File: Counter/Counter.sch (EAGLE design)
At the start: 6 parts

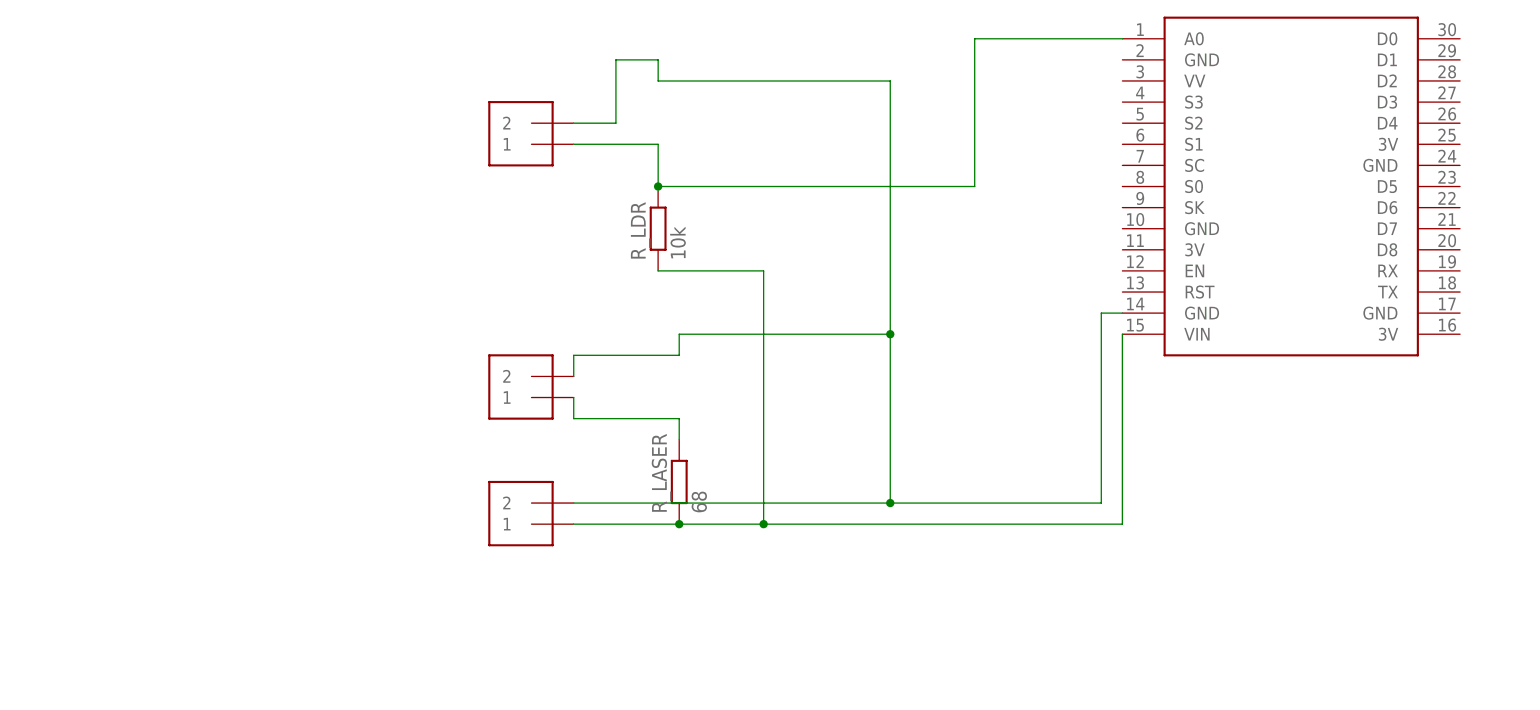
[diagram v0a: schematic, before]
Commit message: revisi rangkaian rev 3 + penambahan reset
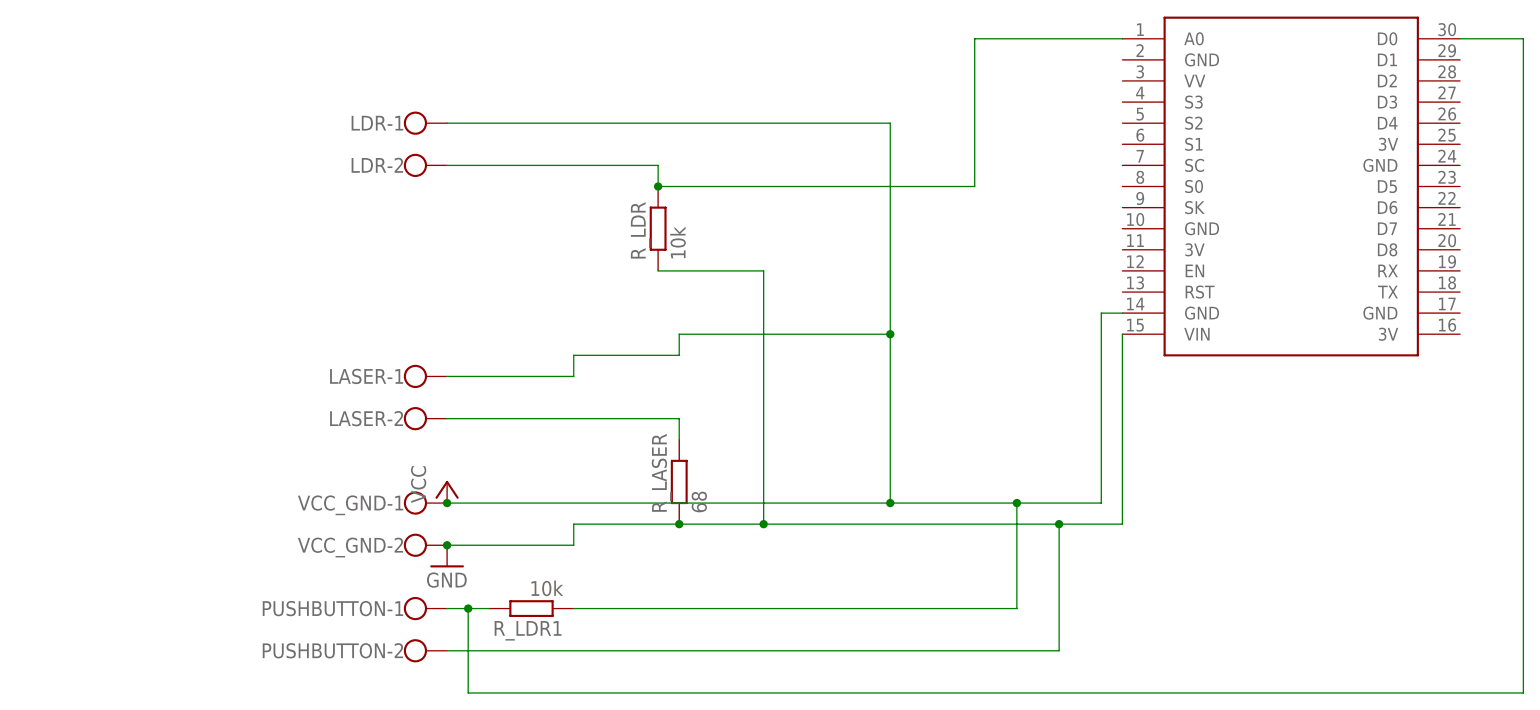
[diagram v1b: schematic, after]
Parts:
- added PUSHBUTTON: (no value), con-wago-500:W237-102
- added R_LDR1: 10k, rcl:R-EU_0207/10
- LASER, LDR, VCC_GND: value 1X2-3.5MM -> (none); device adafruit:1X2-3.5MM -> con-wago-500:W237-102
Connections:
- removed net GROUND: LASER.2, LDR.2, U$1.GND@2, VCC_GND.2
- new net GND: PUSHBUTTON-2.KL, R_LASER.1, R_LDR.1, U$1.VIN, VCC_GND-2.KL
- new net N$1: LDR-2.KL, R_LDR.2, U$1.A0
- net N$2: now also LASER-2.KL; no longer LASER.1
- net N$3: now also PUSHBUTTON-1.KL, R_LDR1.2, U$1.D0; no longer LDR.1, R_LDR.2, U$1.A0
- net VCC: now also LASER-1.KL, LDR-1.KL, R_LDR1.1, U$1.GND@2, VCC_GND-1.KL; no longer R_LASER.1, R_LDR.1, U$1.VIN, VCC_GND.1

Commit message: penambahan fuse dan lampu indikator pada board, pembuatan masking. penambahan program counter
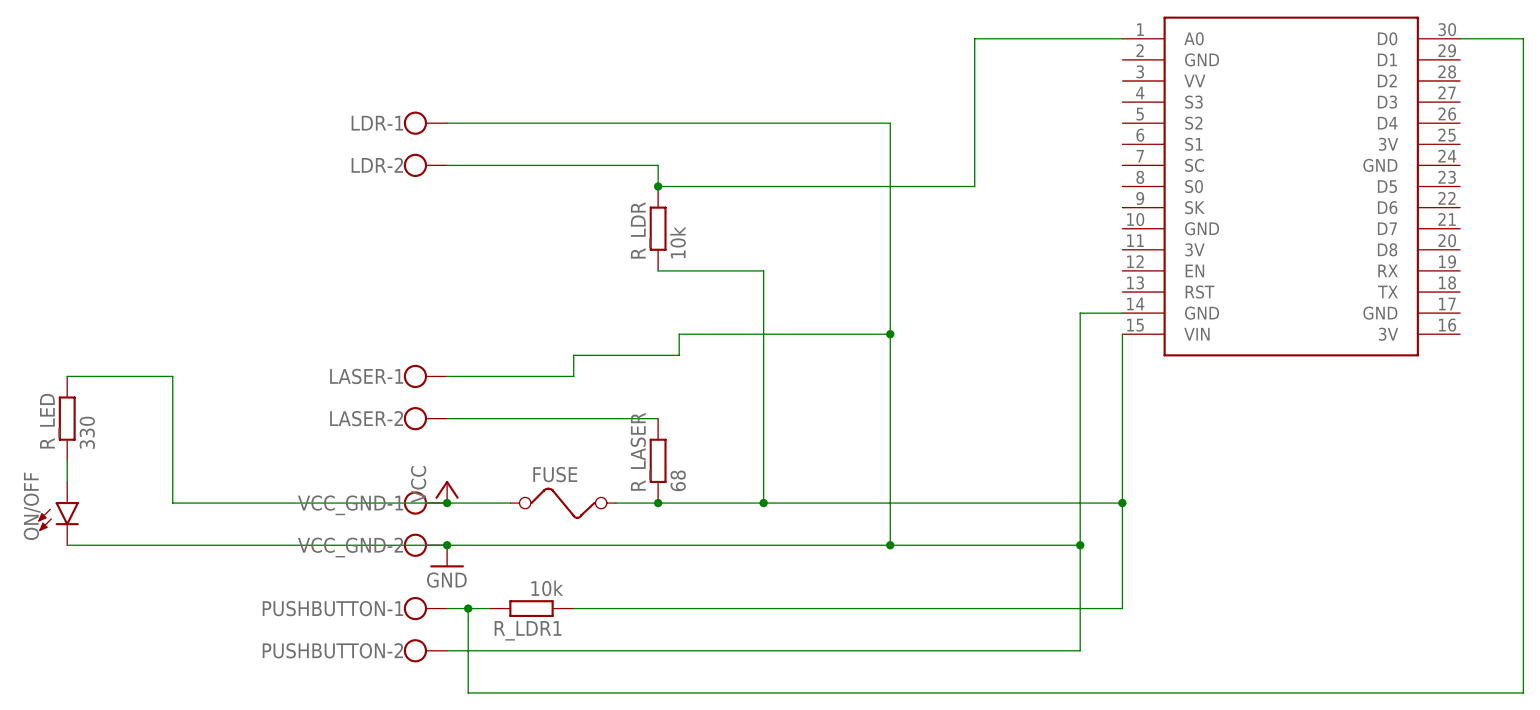
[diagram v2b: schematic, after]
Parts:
- added FUSE: (no value), special:FUSE
- added ON/OFF: (no value), SparkFun-LED:LED5MM
- added R_LED: 330, rcl:R-EU_0207/10
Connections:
- new net N$4: FUSE.2, R_LASER.1, R_LDR.1, R_LDR1.1, U$1.VIN
- new net N$5: ON/OFF.A, R_LED.1
- net GND: now also LASER-1.KL, LDR-1.KL, ON/OFF.C, U$1.GND@2; no longer R_LASER.1, R_LDR.1, U$1.VIN
- net VCC: now also FUSE.1, R_LED.2; no longer LASER-1.KL, LDR-1.KL, R_LDR1.1, U$1.GND@2
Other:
- moved on the sheet: R_LASER
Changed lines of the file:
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@@
 <part name="U$2" library="Evllve PCB Array" library_urn="urn:adsk.eagle:library:14885710" deviceset="VCC" device=""/>
 <part name="GND1" library="PulseOximeterECG_AU" library_urn="urn:adsk.eagle:library:14846661" deviceset="GND" device=""/>
+<part name="FUSE" library="special" library_urn="urn:adsk.eagle:library:367" deviceset="FUSE" device="" package3d_urn="urn:adsk.eagle:package:26650/1"/>
+<part name="ON/OFF" library="SparkFun-LED" library_urn="urn:adsk.eagle:library:529" deviceset="LED" device="5MM" package3d_urn="urn:adsk.eagle:package:39353/1"/>
+<part name="R_LED" library="rcl" library_urn="urn:adsk.eagle:library:334" deviceset="R-EU_" device="0207/10" package3d_urn="urn:adsk.eagle:package:23491/2" value="330"/>
 </parts>
 <sheets>
@@
 <instances>
 <instance part="U$1" gate="G$1" x="66.04" y="53.34" smashed="yes"/>
-<instance part="R_LASER" gate="G$1" x="-7.62" y="17.78" smashed="yes" rot="R90">
-<attribute name="NAME" x="-9.1186" y="13.97" size="1.778" layer="95" rot="R90"/>
-<attribute name="VALUE" x="-4.318" y="13.97" size="1.778" layer="96" rot="R90"/>
+<instance part="R_LASER" gate="G$1" x="-10.16" y="20.32" smashed="yes" rot="R90">
+<attribute name="NAME" x="-11.6586" y="16.51" size="1.778" layer="95" rot="R90"/>
+<attribute name="VALUE" x="-6.858" y="16.51" size="1.778" layer="96" rot="R90"/>
 </instance>
 <instance part="R_LDR" gate="G$1" x="-10.16" y="48.26" smashed="yes" rot="R90">
@@
 <attribute name="VALUE" x="-38.1" y="5.08" size="1.778" layer="96"/>
 </instance>
+<instance part="FUSE" gate="G$1" x="-20.32" y="15.24" smashed="yes">
+<attribute name="NAME" x="-25.4" y="17.78" size="1.778" layer="95"/>
+<attribute name="VALUE" x="-25.4" y="11.43" size="1.778" layer="96"/>
+</instance>
+<instance part="ON/OFF" gate="G$1" x="-81.28" y="15.24" smashed="yes">
+<attribute name="NAME" x="-84.709" y="10.668" size="1.778" layer="95" font="vector" rot="R90"/>
+<attribute name="VALUE" x="-79.375" y="10.668" size="1.778" layer="96" font="vector" rot="R90" align="top-left"/>
+</instance>
+<instance part="R_LED" gate="G$1" x="-81.28" y="25.4" smashed="yes" rot="R90">
+<attribute name="NAME" x="-82.7786" y="21.59" size="1.778" layer="95" rot="R90"/>
+<attribute name="VALUE" x="-77.978" y="21.59" size="1.778" layer="96" rot="R90"/>
+</instance>
 </instances>
 <busses>
@@
 <segment>
 <pinref part="R_LASER" gate="G$1" pin="2"/>
-<wire x1="-7.62" y1="25.4" x2="-7.62" y2="22.86" width="0.1524" layer="91"/>
 <pinref part="LASER" gate="-2" pin="KL"/>
-<wire x1="-35.56" y1="25.4" x2="-7.62" y2="25.4" width="0.1524" layer="91"/>
+<wire x1="-35.56" y1="25.4" x2="-10.16" y2="25.4" width="0.1524" layer="91"/>
 </segment>
 </net>
 <net name="VCC" class="1">
 <segment>
-<wire x1="17.78" y1="60.96" x2="17.78" y2="35.56" width="0.1524" layer="91"/>
-<wire x1="17.78" y1="35.56" x2="17.78" y2="15.24" width="0.1524" layer="91"/>
-<wire x1="17.78" y1="15.24" x2="-35.56" y2="15.24" width="0.1524" layer="91"/>
-<wire x1="-20.32" y1="33.02" x2="-7.62" y2="33.02" width="0.1524" layer="91"/>
-<wire x1="-20.32" y1="30.48" x2="-20.32" y2="33.02" width="0.1524" layer="91"/>
-<wire x1="-7.62" y1="33.02" x2="-7.62" y2="35.56" width="0.1524" layer="91"/>
-<wire x1="-7.62" y1="35.56" x2="17.78" y2="35.56" width="0.1524" layer="91"/>
-<junction x="17.78" y="35.56"/>
-<pinref part="U$1" gate="G$1" pin="GND@2"/>
-<wire x1="45.72" y1="38.1" x2="43.18" y2="38.1" width="0.1524" layer="91"/>
-<wire x1="43.18" y1="38.1" x2="43.18" y2="15.24" width="0.1524" layer="91"/>
-<junction x="17.78" y="15.24"/>
-<pinref part="LASER" gate="-1" pin="KL"/>
-<wire x1="43.18" y1="15.24" x2="33.02" y2="15.24" width="0.1524" layer="91"/>
-<wire x1="33.02" y1="15.24" x2="17.78" y2="15.24" width="0.1524" layer="91"/>
-<wire x1="-35.56" y1="30.48" x2="-20.32" y2="30.48" width="0.1524" layer="91"/>
 <pinref part="VCC_GND" gate="-1" pin="KL"/>
-<pinref part="LDR" gate="-1" pin="KL"/>
-<wire x1="-35.56" y1="60.96" x2="17.78" y2="60.96" width="0.1524" layer="91"/>
 <pinref part="U$2" gate="G$1" pin="VCC"/>
 <junction x="-35.56" y="15.24"/>
-<pinref part="R_LDR1" gate="G$1" pin="1"/>
-<wire x1="-20.32" y1="2.54" x2="33.02" y2="2.54" width="0.1524" layer="91"/>
-<wire x1="33.02" y1="2.54" x2="33.02" y2="15.24" width="0.1524" layer="91"/>
-<junction x="33.02" y="15.24"/>
+<wire x1="-27.94" y1="15.24" x2="-35.56" y2="15.24" width="0.1524" layer="91"/>
+<pinref part="FUSE" gate="G$1" pin="1"/>
+<pinref part="R_LED" gate="G$1" pin="2"/>
+<wire x1="-81.28" y1="30.48" x2="-68.58" y2="30.48" width="0.1524" layer="91"/>
+<wire x1="-68.58" y1="30.48" x2="-68.58" y2="15.24" width="0.1524" layer="91"/>
+<wire x1="-68.58" y1="15.24" x2="-35.56" y2="15.24" width="0.1524" layer="91"/>
 </segment>
 </net>
@@
 <net name="GND" class="1">
 <segment>
-<pinref part="R_LASER" gate="G$1" pin="1"/>
-<wire x1="-7.62" y1="12.7" x2="-20.32" y2="12.7" width="0.1524" layer="91"/>
-<pinref part="U$1" gate="G$1" pin="VIN"/>
-<wire x1="45.72" y1="35.56" x2="45.72" y2="12.7" width="0.1524" layer="91"/>
-<wire x1="45.72" y1="12.7" x2="38.1" y2="12.7" width="0.1524" layer="91"/>
-<junction x="-7.62" y="12.7"/>
-<pinref part="R_LDR" gate="G$1" pin="1"/>
-<wire x1="38.1" y1="12.7" x2="2.54" y2="12.7" width="0.1524" layer="91"/>
-<wire x1="2.54" y1="12.7" x2="-7.62" y2="12.7" width="0.1524" layer="91"/>
-<wire x1="-10.16" y1="43.18" x2="2.54" y2="43.18" width="0.1524" layer="91"/>
-<wire x1="2.54" y1="43.18" x2="2.54" y2="12.7" width="0.1524" layer="91"/>
-<junction x="2.54" y="12.7"/>
 <pinref part="VCC_GND" gate="-2" pin="KL"/>
-<wire x1="-35.56" y1="10.16" x2="-20.32" y2="10.16" width="0.1524" layer="91"/>
-<wire x1="-20.32" y1="10.16" x2="-20.32" y2="12.7" width="0.1524" layer="91"/>
 <pinref part="GND1" gate="1" pin="GND"/>
 <junction x="-35.56" y="10.16"/>
+<wire x1="-35.56" y1="10.16" x2="17.78" y2="10.16" width="0.1524" layer="91"/>
+<pinref part="U$1" gate="G$1" pin="GND@2"/>
+<wire x1="17.78" y1="10.16" x2="40.64" y2="10.16" width="0.1524" layer="91"/>
+<wire x1="40.64" y1="10.16" x2="40.64" y2="38.1" width="0.1524" layer="91"/>
+<wire x1="40.64" y1="38.1" x2="45.72" y2="38.1" width="0.1524" layer="91"/>
+<pinref part="LDR" gate="-1" pin="KL"/>
+<wire x1="-35.56" y1="60.96" x2="17.78" y2="60.96" width="0.1524" layer="91"/>
+<wire x1="17.78" y1="60.96" x2="17.78" y2="35.56" width="0.1524" layer="91"/>
+<wire x1="-7.62" y1="35.56" x2="17.78" y2="35.56" width="0.1524" layer="91"/>
+<wire x1="-7.62" y1="33.02" x2="-7.62" y2="35.56" width="0.1524" layer="91"/>
+<wire x1="-20.32" y1="33.02" x2="-7.62" y2="33.02" width="0.1524" layer="91"/>
+<wire x1="-20.32" y1="30.48" x2="-20.32" y2="33.02" width="0.1524" layer="91"/>
+<pinref part="LASER" gate="-1" pin="KL"/>
+<wire x1="-35.56" y1="30.48" x2="-20.32" y2="30.48" width="0.1524" layer="91"/>
+<wire x1="17.78" y1="35.56" x2="17.78" y2="10.16" width="0.1524" layer="91"/>
+<junction x="17.78" y="35.56"/>
+<junction x="17.78" y="10.16"/>
 <pinref part="PUSHBUTTON" gate="-2" pin="KL"/>
-<wire x1="-35.56" y1="-2.54" x2="38.1" y2="-2.54" width="0.1524" layer="91"/>
-<wire x1="38.1" y1="12.7" x2="38.1" y2="-2.54" width="0.1524" layer="91"/>
-<junction x="38.1" y="12.7"/>
+<wire x1="-35.56" y1="-2.54" x2="40.64" y2="-2.54" width="0.1524" layer="91"/>
+<wire x1="40.64" y1="-2.54" x2="40.64" y2="10.16" width="0.1524" layer="91"/>
+<junction x="40.64" y="10.16"/>
+<pinref part="ON/OFF" gate="G$1" pin="C"/>
+<wire x1="-81.28" y1="10.16" x2="-35.56" y2="10.16" width="0.1524" layer="91"/>
 </segment>
 </net>
@@
 </segment>
 </net>
+<net name="N$4" class="1">
+<segment>
+<wire x1="2.54" y1="15.24" x2="-10.16" y2="15.24" width="0.1524" layer="91"/>
+<wire x1="2.54" y1="15.24" x2="45.72" y2="15.24" width="0.1524" layer="91"/>
+<pinref part="U$1" gate="G$1" pin="VIN"/>
+<wire x1="45.72" y1="15.24" x2="45.72" y2="35.56" width="0.1524" layer="91"/>
+<pinref part="R_LASER" gate="G$1" pin="1"/>
+<junction x="-10.16" y="15.24"/>
+<pinref part="R_LDR" gate="G$1" pin="1"/>
+<wire x1="-10.16" y1="43.18" x2="2.54" y2="43.18" width="0.1524" layer="91"/>
+<wire x1="2.54" y1="43.18" x2="2.54" y2="15.24" width="0.1524" layer="91"/>
+<junction x="2.54" y="15.24"/>
+<pinref part="R_LDR1" gate="G$1" pin="1"/>
+<wire x1="-20.32" y1="2.54" x2="45.72" y2="2.54" width="0.1524" layer="91"/>
+<wire x1="45.72" y1="2.54" x2="45.72" y2="15.24" width="0.1524" layer="91"/>
+<junction x="45.72" y="15.24"/>
+<wire x1="-10.16" y1="15.24" x2="-15.24" y2="15.24" width="0.1524" layer="91"/>
+<pinref part="FUSE" gate="G$1" pin="2"/>
+</segment>
+</net>
+<net name="N$5" class="0">
+<segment>
+<pinref part="R_LED" gate="G$1" pin="1"/>
+<pinref part="ON/OFF" gate="G$1" pin="A"/>
+<wire x1="-81.28" y1="20.32" x2="-81.28" y2="17.78" width="0.1524" layer="91"/>
+</segment>
+</net>
 </nets>
 </sheet>
 </sheets>
+<errors>
+</errors>
 </schematic>
 </drawing>

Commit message: penambahan reset counter
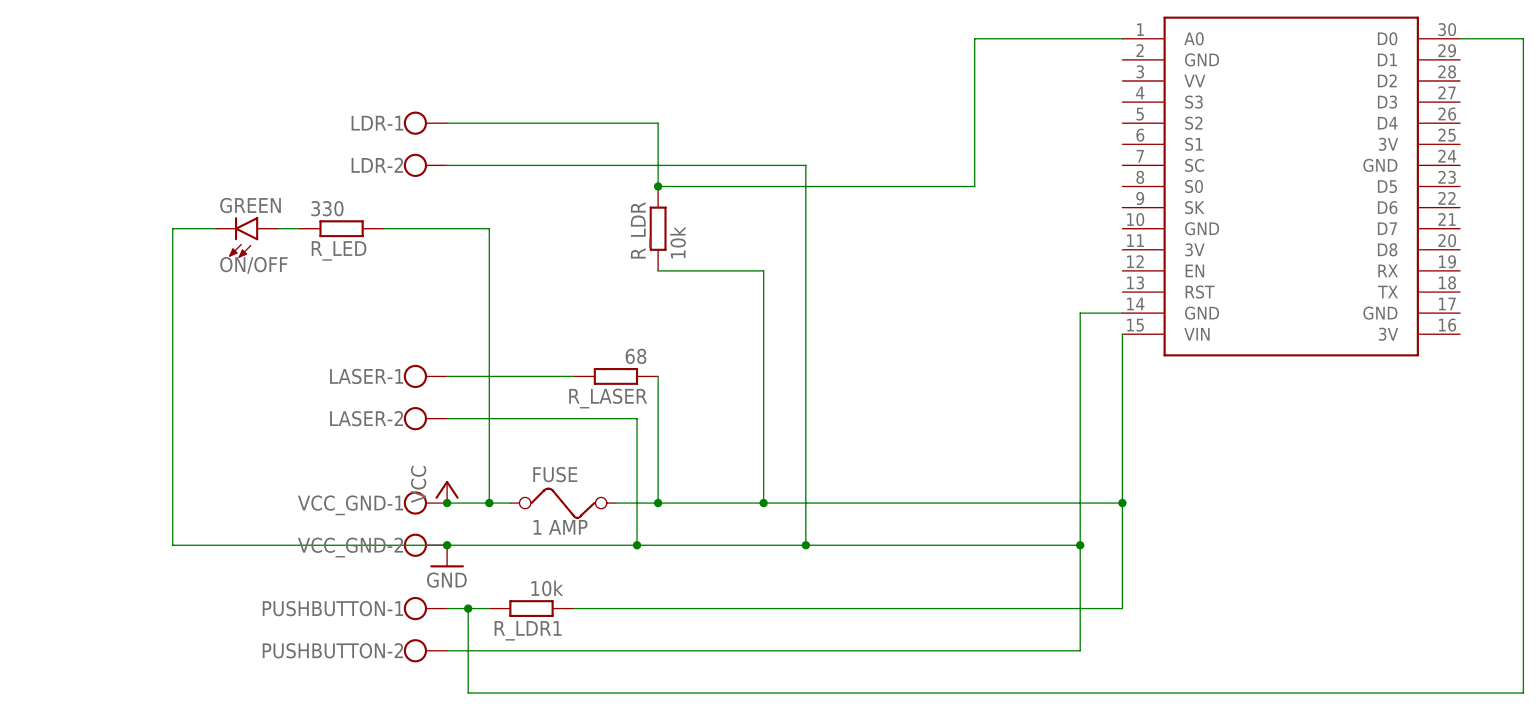
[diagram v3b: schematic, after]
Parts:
- FUSE: value (none) -> 1 AMP
- ON/OFF: value (none) -> GREEN
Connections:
- net GND: now also LASER-2.KL, LDR-2.KL; no longer LASER-1.KL, LDR-1.KL
- net N$1: now also LDR-1.KL; no longer LDR-2.KL
- net N$2: now also LASER-1.KL; no longer LASER-2.KL
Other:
- moved on the sheet: ON/OFF, R_LASER, R_LED
